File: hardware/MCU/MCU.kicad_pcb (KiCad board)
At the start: 2 copper layers, 40 x 40 mm, 46 parts, among them P1 CONN_01X05, P2 CONN_01X04, P3 CONN_01X05, P4 CONN_01X05, U1 MAX6369, U2 TC1262-30VDB, U3 DS18B20, U4 PIC18F45K22, U5 LT6005, Y1 Crystal

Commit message: - Esquematicos generados - Archivos de fabricacion - BOM para Farnell
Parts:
- removed G?: LOGO, imagenes:amsat-satelite-recortada-fondo-30
- added G***: LOGO, imagenes:amsat-palabra-70, F.Cu at (24.5, 189.5)
- moved FID3 38.7 mm to (44.5, 196.1)
- moved FID2 10.4 mm to (19.5, 190.9)
- moved FID1 3.09 mm to (14.7, 159.6)
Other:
- board text added: "nmendi"

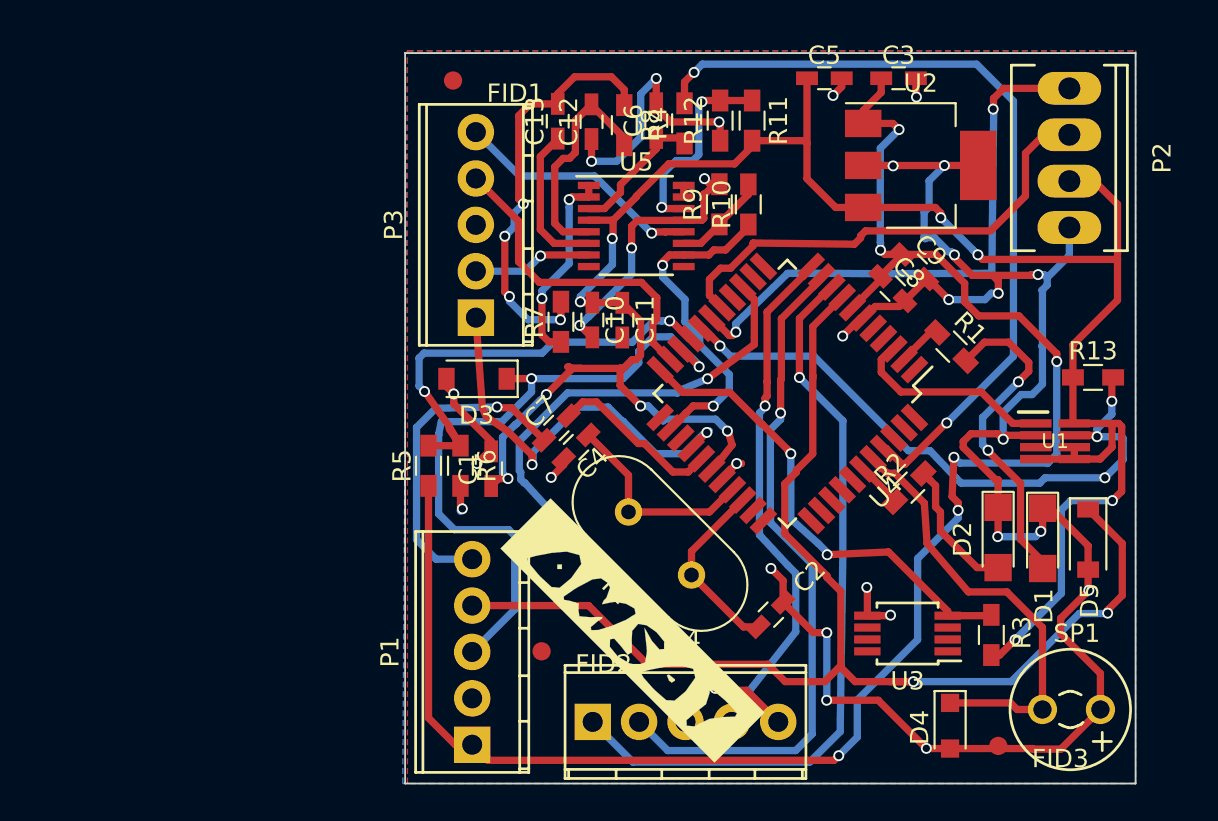
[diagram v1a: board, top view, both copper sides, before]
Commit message: Added 3D models of header connectors
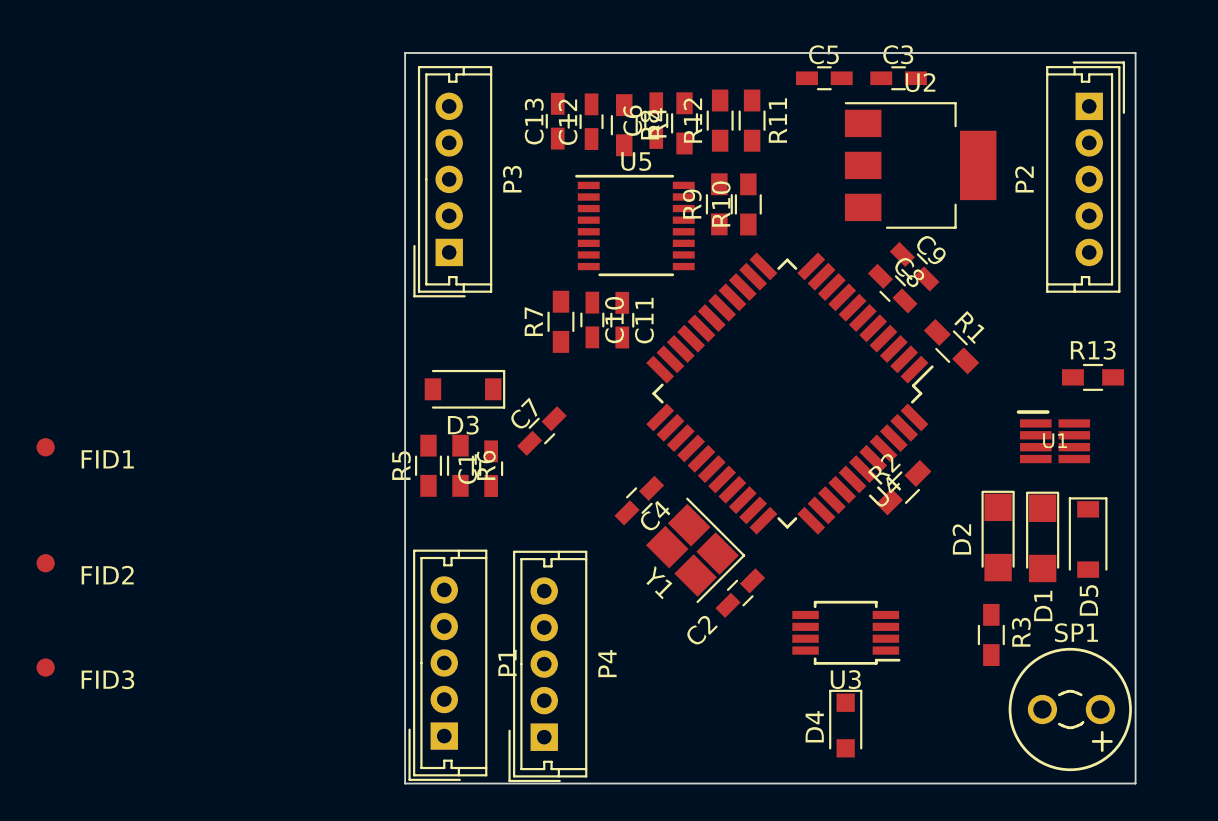
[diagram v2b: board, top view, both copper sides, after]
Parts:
- removed G***: LOGO, imagenes:amsat-palabra-70
- P1, P3, P4: footprint Connectors_Terminal_Blocks:TerminalBlock_Pheonix_MPT-2.54mm_5pol -> Connectors_Molex:Molex_MicroLatch-53253-0570_05x2.00mm_Straight
- P2: value CONN_01X04 -> CONN_01X05; footprint Sockets_MOLEX_KK-System:Socket_MOLEX-KK-RM2-54mm_Lock_4pin_straight -> Connectors_Molex:Molex_MicroLatch-53253-0570_05x2.00mm_Straight
- R11, R12, R9: value R -> 1K
- U2: footprint SOT-223 -> TO_SOT_Packages_SMD:SOT-223
- Y1: footprint Crystals:Crystal_HC49-4H_Vertical -> Crystals:Crystal_SMD_EuroQuartz_X22-4pin_2.5x2.0mm_HandSoldering
- moved FID3 52.3 mm to (-7.62, 191.8)
- moved FID1 30.0 mm to (-7.62, 179.7)
- moved FID2 27.6 mm to (-7.62, 186.1)
- moved D4 5.72 mm to (36.2, 194.9)
- moved C4 4.54 mm to (24.9, 182.6)
- moved P3 3.86 mm to (14.5, 169.0)
- moved U3 3.39 mm to (36.2, 189.9)
- moved P2 3.03 mm to (49.5, 161.0)
- moved P4 2.78 mm to (19.7, 195.6), turned to 90 degrees
- moved C2 2.05 mm to (30.4, 187.7), turned to 225 degrees
- moved P1 1.60 mm to (14.2, 195.5)
- moved Y1 1.35 mm to (27.8, 185.3)
- moved D3 0.94 mm to (15.2, 176.5)
- moved C7 0.81 mm to (19.6, 178.8)
- moved R2 0.30 mm to (39.4, 181.9)
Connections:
- C8 pad 1: VDD -> VCC
- C9 pad 1: VDD -> VCC
- P2 pad 1: /PGD -> /~WDO/MCLR
- P2 pad 2: /PGC -> VCC
- P2 pad 3: VCC -> GND
- P2 pad 4: GND -> /PGD
- R13 pad 2: /~WDO -> /~WDO/MCLR
- R3 pad 1: VCC -> /TEMP
- R3 pad 2: /TEMP -> VCC
- U1 pad 7: /~WDO -> /~WDO/MCLR
- U4 pad 18: /~WDO -> /~WDO/MCLR
- U4 pad 7: VDD -> VCC
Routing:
- net GND: track 143.1 -> 0.00 mm, vias 30 -> 0
- net VCC: track 116.3 -> 0.00 mm, vias 10 -> 0
- net VDD: track 95.7 -> 0.00 mm, vias 6 -> 0
- net /PWD: track 69.9 -> 0.00 mm, vias 2 -> 0
- net /BEACON_ON: track 44.3 -> 0.00 mm, vias 2 -> 0
- net /PTT: track 41.3 -> 0.00 mm, vias 1 -> 0
- net /BEACON_MODE: track 40.5 -> 0.00 mm, vias 2 -> 0
- net /RPT: track 37.7 -> 0.00 mm, vias 1 -> 0
- net /SOL: track 37.5 -> 0.00 mm, vias 2 -> 0
- net /~WDO: track 34.8 -> 0.00 mm, vias 4 -> 0
- net /PGD: track 31.4 -> 0.00 mm, vias 2 -> 0
- net /HIPWR: track 28.1 -> 0.00 mm, vias 1 -> 0
- net /PGC: track 26.4 -> 0.00 mm
- net /TEMP: track 26.2 -> 0.00 mm, vias 2 -> 0
- net /VBAT: track 24.7 -> 0.00 mm, vias 2 -> 0
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- removed copper zone on B.Cu, net GND
- removed copper zone on F.Cu, net GND

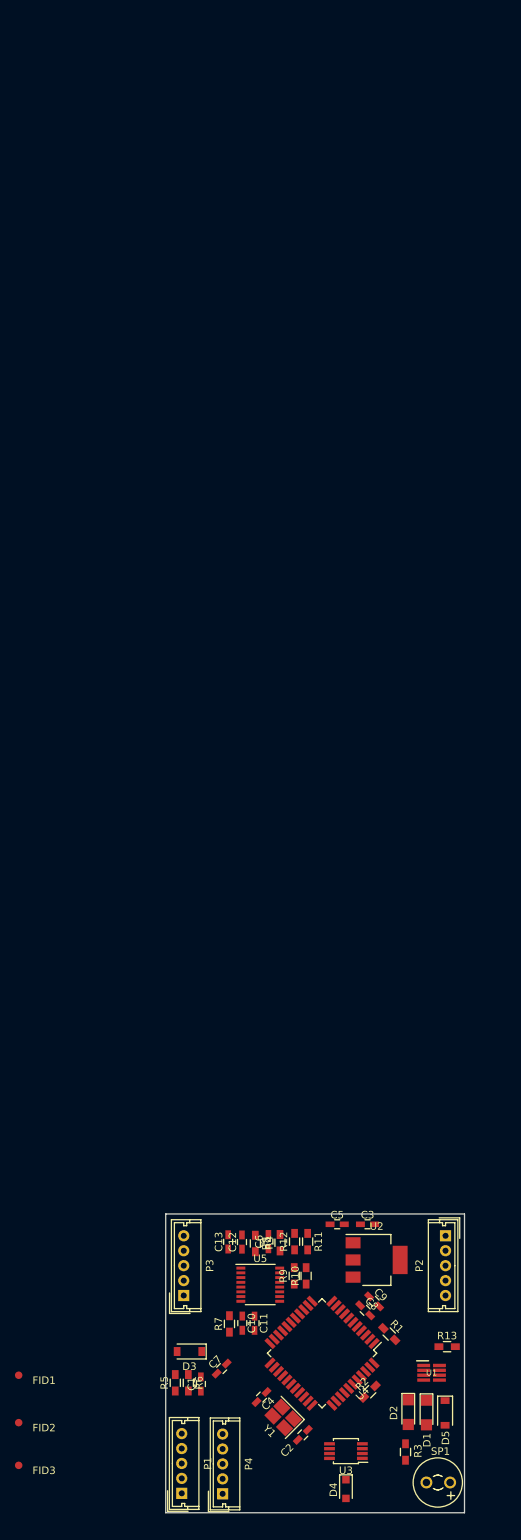
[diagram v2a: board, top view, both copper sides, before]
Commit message: Placement terminado para la versión 2.0 de la MCU
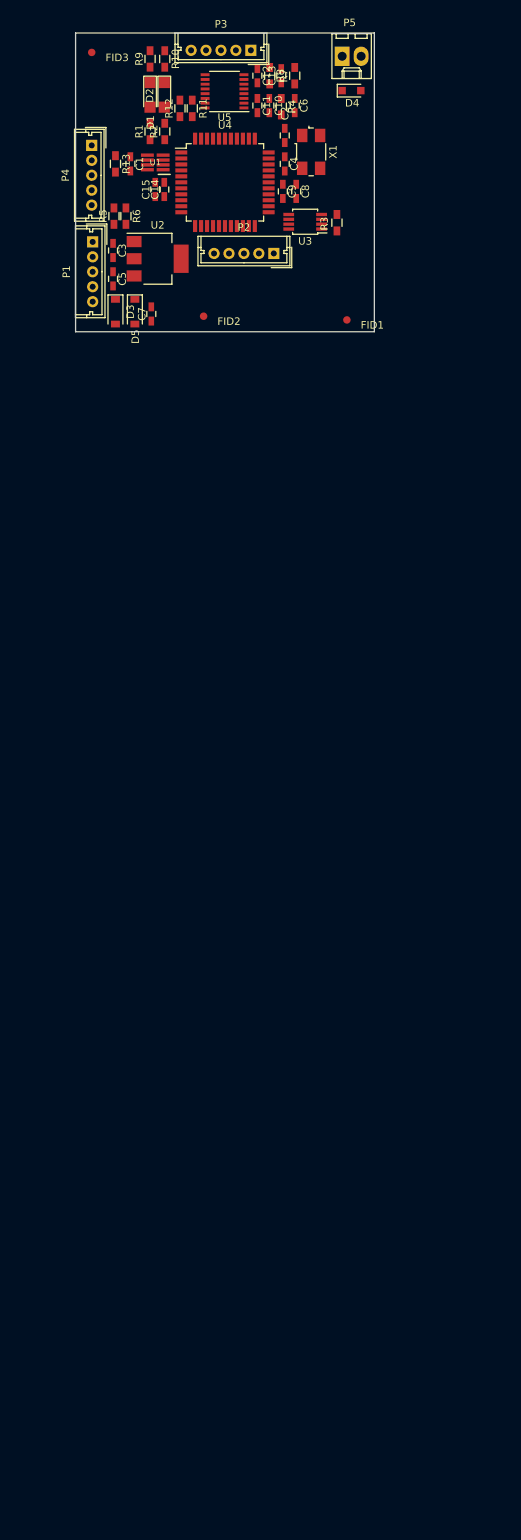
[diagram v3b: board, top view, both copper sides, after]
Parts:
- removed SP1: SPEAKER, Buzzers_Beepers:MagneticBuzzer_Kingstate_KCG0601
- removed Y1: Crystal, Crystals:Crystal_SMD_EuroQuartz_X22-4pin_2.5x2.0mm_HandSoldering
- added C14: 10nF, Capacitors_SMD:C_0603_HandSoldering, F.Cu at (11.9, 21.0)
- added C15: 100nF, Capacitors_SMD:C_0603_HandSoldering, F.Cu at (10.7, 21.0)
- added P5: CONN_01X02, Connectors_Molex:Molex_KK-6410-02_02x2.54mm_Straight, F.Cu at (35.7, 3.12)
- added X1: CRYSTAL_SMD, Crystals:Crystal_SMD_0603-4pin_6.0x3.5mm, F.Cu at (31.5, 15.9)
- moved FID3 189.4 mm to (2.16, 2.60)
- moved D4 187.2 mm to (36.9, 7.72), turned to 0 degrees
- moved P4 181.4 mm to (2.16, 15.1), turned to 270 degrees
- moved D1 180.3 mm to (9.97, 8.28)
- moved D2 179.4 mm to (11.9, 8.28)
- moved C2 174.0 mm to (28.0, 13.7), turned to 90 degrees
- moved R2 170.9 mm to (11.9, 13.2), turned to 90 degrees
- moved P1 168.0 mm to (2.29, 28.0), turned to 270 degrees
- moved R7 167.3 mm to (29.3, 5.72)
- moved P3 167.0 mm to (23.5, 2.32), turned to 180 degrees
- moved U1 166.2 mm to (10.7, 17.3), turned to 180 degrees
- moved C4 165.1 mm to (28.0, 17.5), turned to 270 degrees
- moved R3 164.8 mm to (35.0, 25.4), turned to 270 degrees
- moved U3 164.7 mm to (30.7, 25.3)
- moved R13 164.5 mm to (5.34, 17.5), turned to 270 degrees
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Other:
- rule via_min_size: 0.4 -> 0.6
